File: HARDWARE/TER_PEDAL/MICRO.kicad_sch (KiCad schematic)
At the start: 22 parts, among them J1 DEBUG, SW1 RST, U1 STM32F103C8Tx, Y1 8mHz

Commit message: Initial Layout Finished
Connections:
- net APPS_1_ADC: now also U1.16 (PA6); no longer U1.10 (PA0)
- net APPS_2_ADC: now also U1.17 (PA7); no longer U1.11 (PA1)
- net BPPS_ADC: now also U1.19 (PB1); no longer U1.12 (PA2)
- net DBG_LED: now also U1.14 (PA4); no longer U1.40 (PB4)
- net IMP_LED: now also U1.13 (PA3); no longer U1.39 (PB3)
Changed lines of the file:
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@@
+    (stroke (width 0) (type default))
+  )
+  (wire (pts (xy 158.75 66.04) (xy 161.29 66.04))
     (stroke (width 0) (type default))
   )
@@
     (stroke (width 0) (type default))
   )
+  (wire (pts (xy 158.75 68.58) (xy 161.29 68.58))
+    (stroke (width 0) (type default))
+  )
   (wire (pts (xy 22.86 80.01) (xy 22.86 78.74))
     (stroke (width 0) (type default))
@@
     (stroke (width 0) (type default))
   )
+  (wire (pts (xy 125.73 81.28) (xy 118.11 81.28))
+    (stroke (width 0) (type default))
+  )
   (wire (pts (xy 138.43 43.18) (xy 140.97 43.18))
     (stroke (width 0) (type default))
@@
     (stroke (width 0) (type default))
   )
-  (wire (pts (xy 160.02 55.88) (xy 158.75 55.88))
-    (stroke (width 0) (type default))
-  )
   (wire (pts (xy 148.59 41.91) (xy 148.59 45.72))
     (stroke (width 0) (type default))
   )
+  (wire (pts (xy 161.29 60.96) (xy 158.75 60.96))
+    (stroke (width 0) (type default))
+  )
   (wire (pts (xy 26.67 157.48) (xy 26.67 146.05))
     (stroke (width 0) (type default))
@@
     (stroke (width 0) (type default))
   )
-  (wire (pts (xy 160.02 53.34) (xy 158.75 53.34))
-    (stroke (width 0) (type default))
-  )
   (wire (pts (xy 256.54 33.02) (xy 259.08 33.02))
     (stroke (width 0) (type default))
@@
     (stroke (width 0) (type default))
   )
+  (wire (pts (xy 161.29 58.42) (xy 158.75 58.42))
+    (stroke (width 0) (type default))
+  )
   (wire (pts (xy 33.02 114.3) (xy 33.02 111.76))
     (stroke (width 0) (type default))
@@
   )
   (polyline (pts (xy 52.07 128.27) (xy 52.07 198.12))
-    (stroke (width 0) (type default))
-  )
-  (wire (pts (xy 160.02 50.8) (xy 158.75 50.8))
     (stroke (width 0) (type default))
   )
@@
     (effects (font (size 1.27 1.27)) (justify right bottom))
   )
-  (hierarchical_label "DBG_LED" (shape input) (at 125.73 88.9 180) (fields_autoplaced)
+  (hierarchical_label "CAN_RX" (shape input) (at 166.37 78.74 0) (fields_autoplaced)
+    (effects (font (size 1.27 1.27)) (justify left))
+  )
+  (hierarchical_label "APPS_1_ADC" (shape input) (at 161.29 66.04 0) (fields_autoplaced)
+    (effects (font (size 1.27 1.27)) (justify left))
+  )
+  (hierarchical_label "DBG_LED" (shape input) (at 161.29 60.96 0) (fields_autoplaced)
+    (effects (font (size 1.27 1.27)) (justify left))
+  )
+  (hierarchical_label "BPPS_ADC" (shape input) (at 118.11 81.28 180) (fields_autoplaced)
     (effects (font (size 1.27 1.27)) (justify right))
   )
-  (hierarchical_label "CAN_RX" (shape input) (at 166.37 78.74 0) (fields_autoplaced)
-    (effects (font (size 1.27 1.27)) (justify left))
-  )
-  (hierarchical_label "APPS_2_ADC" (shape input) (at 160.02 53.34 0) (fields_autoplaced)
-    (effects (font (size 1.27 1.27)) (justify left))
-  )
-  (hierarchical_label "APPS_1_ADC" (shape input) (at 160.02 50.8 0) (fields_autoplaced)
-    (effects (font (size 1.27 1.27)) (justify left))
-  )
-  (hierarchical_label "IMP_LED" (shape input) (at 125.73 86.36 180) (fields_autoplaced)
-    (effects (font (size 1.27 1.27)) (justify right))
-  )
-  (hierarchical_label "BPPS_ADC" (shape input) (at 160.02 55.88 0) (fields_autoplaced)
-    (effects (font (size 1.27 1.27)) (justify left))
-  )
+  (hierarchical_label "APPS_2_ADC" (shape input) (at 161.29 68.58 0) (fields_autoplaced)
+    (effects (font (size 1.27 1.27)) (justify left))
+  )
+  (hierarchical_label "IMP_LED" (shape input) (at 161.29 58.42 0) (fields_autoplaced)
+    (effects (font (size 1.27 1.27)) (justify left))
+  )

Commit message: Swapped Custom Supply for traco for simplicity
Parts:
- C5: footprint Capacitor_SMD:C_0603_1608Metric -> Capacitor_SMD:C_0805_2012Metric
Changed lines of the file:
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@@
       (effects (font (size 1.27 1.27)) (justify left))
     )
-    (property "Footprint" "Capacitor_SMD:C_0603_1608Metric" (at 15.24 27.94 0)
+    (property "Footprint" "Capacitor_SMD:C_0805_2012Metric" (at 15.24 27.94 0)
       (effects (font (size 1.27 1.27)) hide)
     )

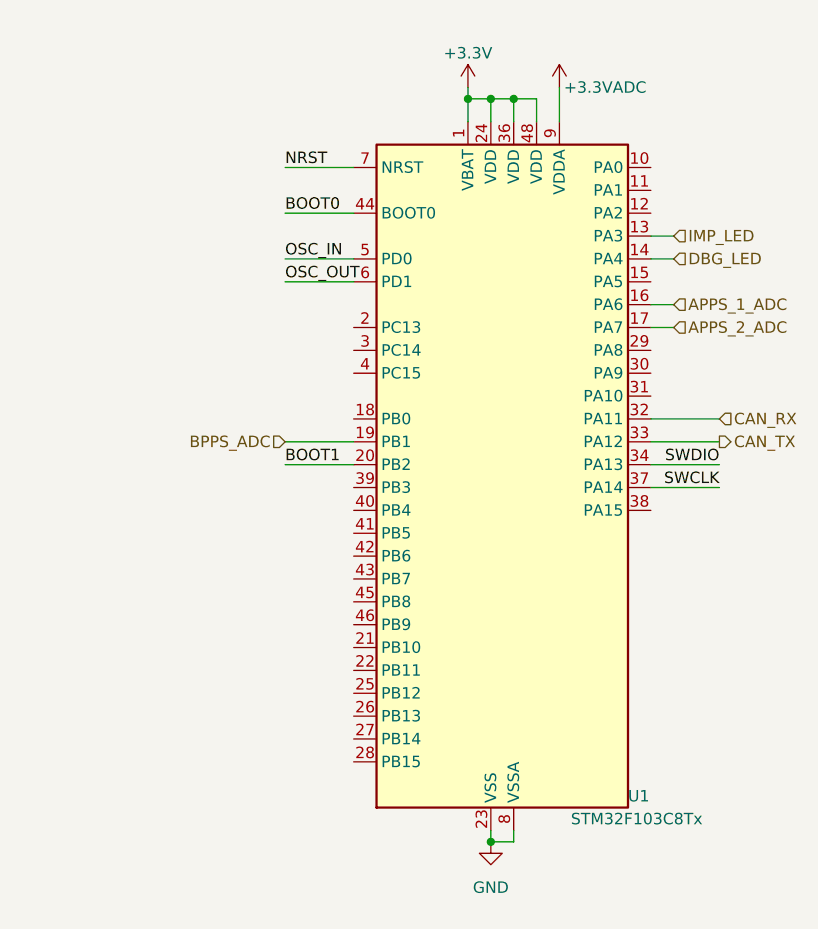
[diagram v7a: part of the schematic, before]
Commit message: Added decouple to all sensors and a new steering sensor input
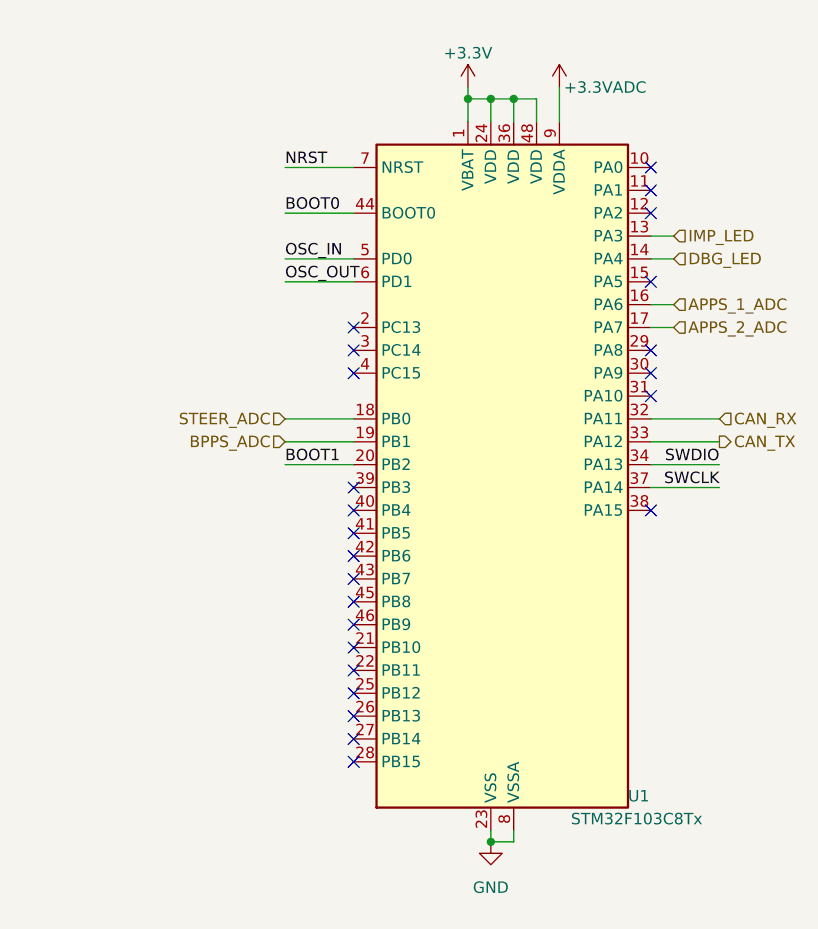
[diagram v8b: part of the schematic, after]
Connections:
- net STEER_ADC: now reaches U1.18 (PB0)
- no-connect marks 0 -> 24
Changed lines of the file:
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@@
   (junction (at 140.97 43.18) (diameter 0) (color 0 0 0 0)
   )
+  (no_connect (at 125.73 96.52))
+  (no_connect (at 125.73 111.76))
+  (no_connect (at 125.73 93.98))
+  (no_connect (at 125.73 114.3))
+  (no_connect (at 125.73 99.06))
+  (no_connect (at 158.75 55.88))
+  (no_connect (at 125.73 73.66))
+  (no_connect (at 125.73 101.6))
+  (no_connect (at 125.73 68.58))
+  (no_connect (at 158.75 53.34))
+  (no_connect (at 125.73 71.12))
+  (no_connect (at 158.75 63.5))
+  (no_connect (at 125.73 91.44))
+  (no_connect (at 158.75 76.2))
+  (no_connect (at 158.75 88.9))
+  (no_connect (at 125.73 116.84))
+  (no_connect (at 125.73 88.9))
+  (no_connect (at 125.73 86.36))
+  (no_connect (at 158.75 73.66))
+  (no_connect (at 125.73 106.68))
+  (no_connect (at 125.73 109.22))
+  (no_connect (at 125.73 104.14))
+  (no_connect (at 158.75 50.8))
+  (no_connect (at 158.75 71.12))
   (wire (pts (xy 22.86 30.48) (xy 30.48 30.48))
     (stroke (width 0) (type default))
@@
   )
   (wire (pts (xy 31.75 110.49) (xy 31.75 111.76))
+    (stroke (width 0) (type default))
+  )
+  (wire (pts (xy 118.11 78.74) (xy 125.73 78.74))
     (stroke (width 0) (type default))
   )
@@
     (effects (font (size 1.27 1.27)) (justify right))
   )
+  (hierarchical_label "STEER_ADC" (shape input) (at 118.11 78.74 180) (fields_autoplaced)
+    (effects (font (size 1.27 1.27)) (justify right))
+  )
